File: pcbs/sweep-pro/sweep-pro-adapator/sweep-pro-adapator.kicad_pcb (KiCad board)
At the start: 2 copper layers, 82.9 x 58.6 mm, 19 parts, among them J1 Conn_01x04_Female, J2 Conn_01x04_Female, J3 expantion1, SW1 Val**, SW2 Val**, SW3 Val**, SW4 Val**

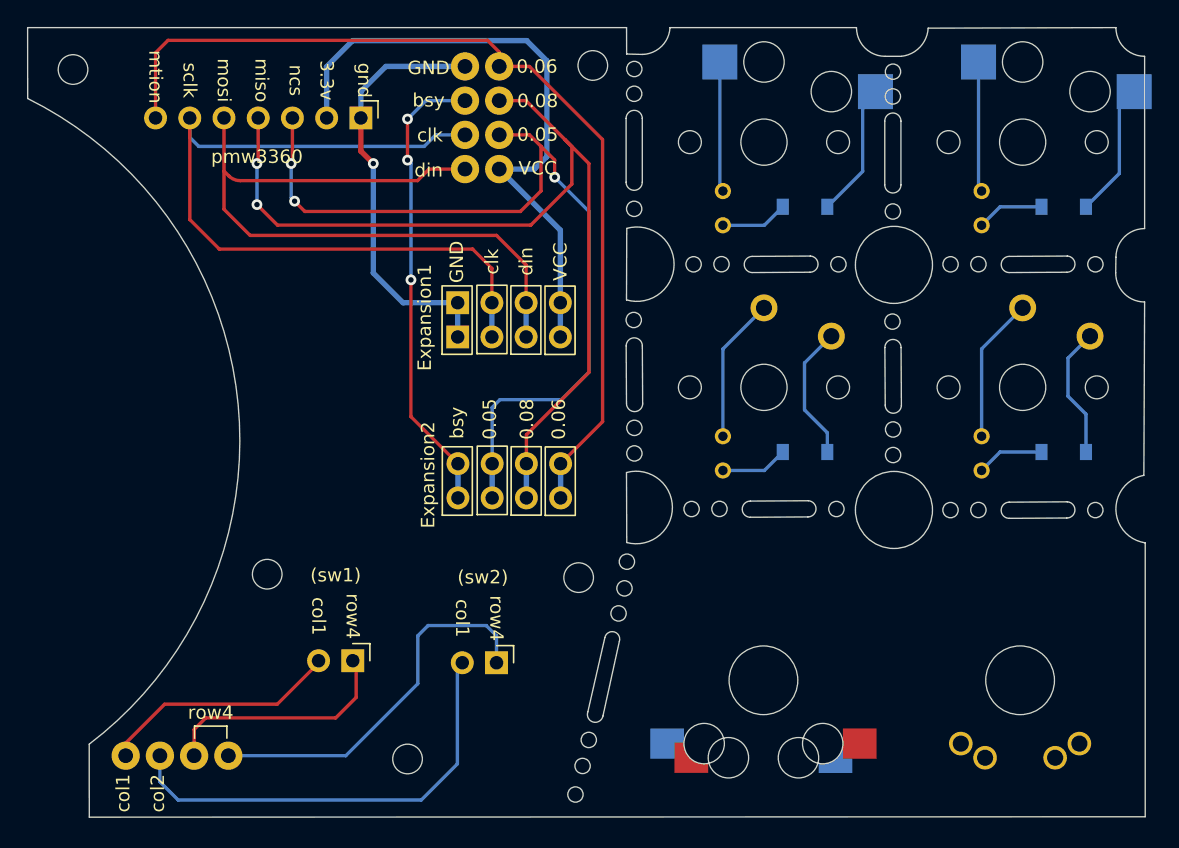
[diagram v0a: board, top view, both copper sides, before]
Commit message: remove extra swithes from sweepro-adaptor due to jlc extra charge
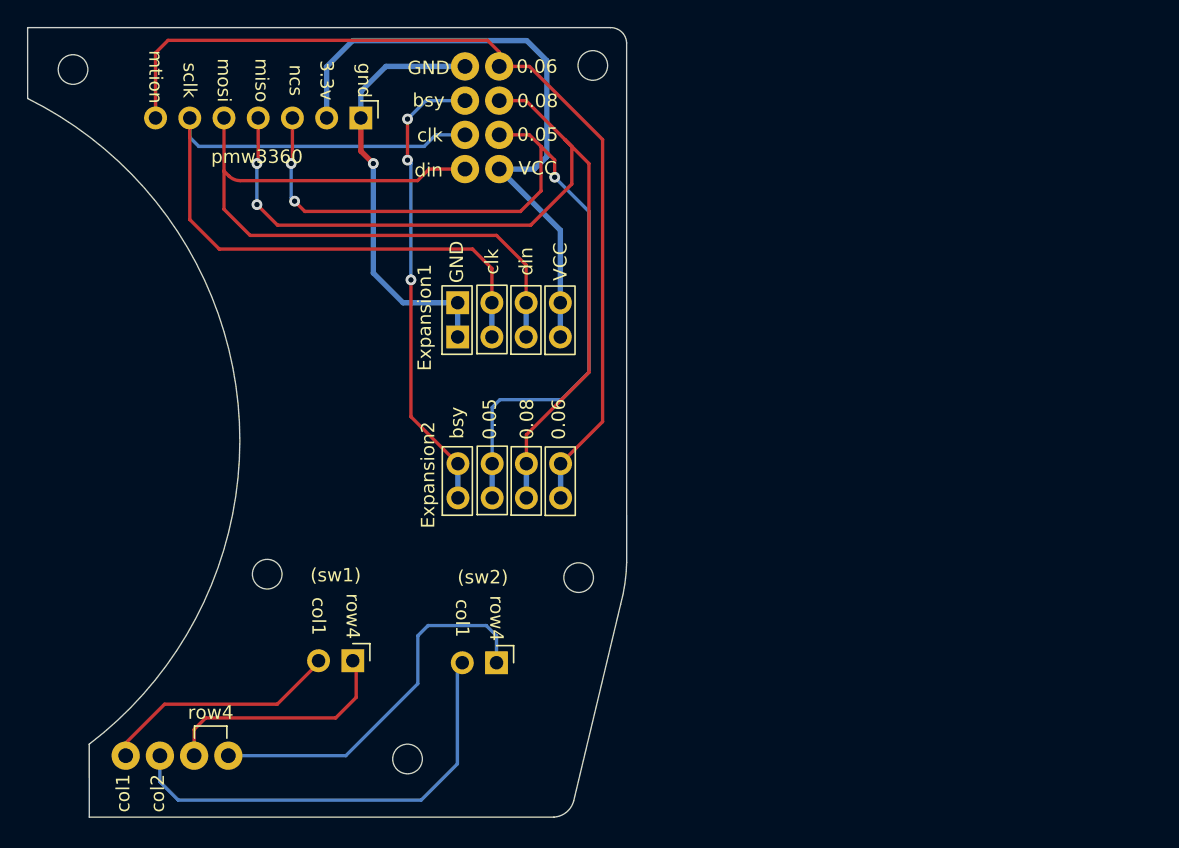
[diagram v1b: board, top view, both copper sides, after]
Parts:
- removed SW**: SW_Push, mylib:gateron-ks27-reversible
- removed SW**: SW_Push, mylib:gateron-ks27-reversible-hotplug
- removed SW1, SW2: Val**, mylib:Kailh_Choc_Hotplug_standalone
- removed SW3, SW4: Val**, mylib:Kailh_Choc_standalone
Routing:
- net (no net): track 631.7 -> 530.7 mm
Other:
- board size 82.9 x 58.6 mm -> 44.5 x 58.6 mm
